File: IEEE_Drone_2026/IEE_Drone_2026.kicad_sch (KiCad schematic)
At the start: 30 parts, among them IC1 TPSM84209RKHT, IC2 TPSM84209RKHT, J1 ESC, J10 M2, J11 Conn_01x02_Socket, J2 M4 Mounting, J3 M4 Mounting, J4 M4 Mounting, J5 M4 Mounting, J6 Pixy2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

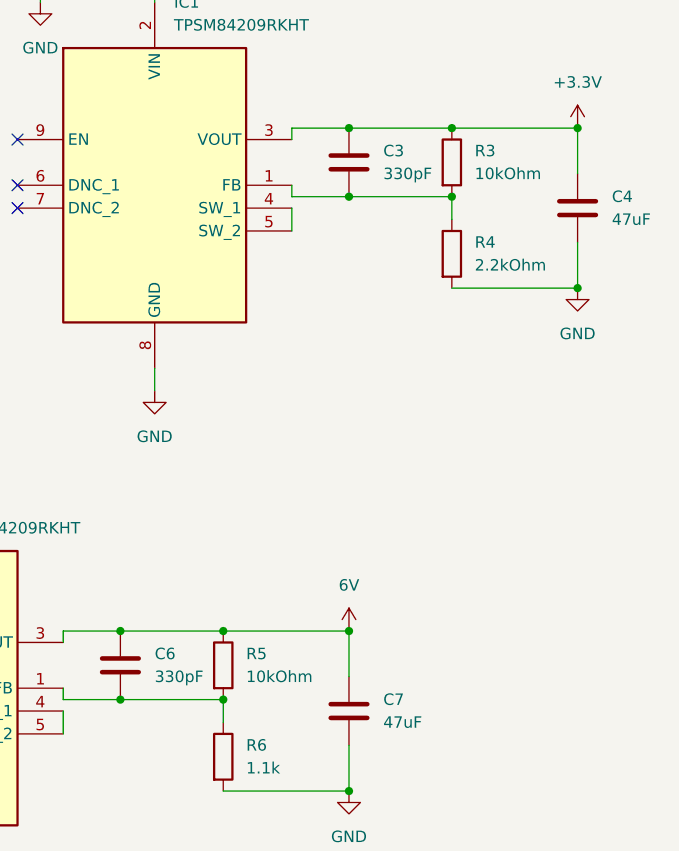
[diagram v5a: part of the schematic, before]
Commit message: updated c4 c5 c7 to 1206
coudn't find 0603 in spec
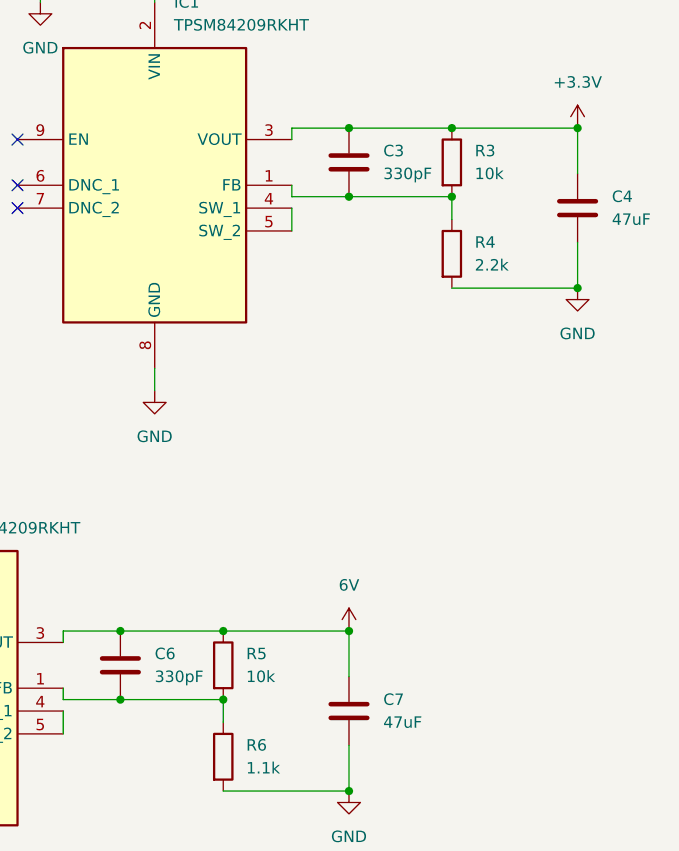
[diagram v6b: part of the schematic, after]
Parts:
- C4, C5, C7: footprint Capacitor_SMD:C_0603_1608Metric_Pad1.08x0.95mm_HandSolder -> Capacitor_SMD:C_1206_3216Metric_Pad1.33x1.80mm_HandSolder
- J1, J10, J11, J2, J3, J4, J5, J6, J7, J8, J9: now left out of the parts list
- Q1: footprint Package_TO_SOT_THT:TO-39-3 -> 2n2222:SOT95P237X111-3N
- R3, R5: value 10kOhm -> 10k
- R4: value 2.2kOhm -> 2.2k
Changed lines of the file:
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@@
 		(unit 1)
 		(exclude_from_sim no)
-		(in_bom yes)
+		(in_bom no)
 		(on_board yes)
 		(dnp no)
@@
 			)
 		)
-		(property "Footprint" "Capacitor_SMD:C_0603_1608Metric_Pad1.08x0.95mm_HandSolder"
+		(property "Footprint" "Capacitor_SMD:C_1206_3216Metric_Pad1.33x1.80mm_HandSolder"
 			(at 200.66 108.2548 0)
 			(effects
@@
 		(unit 1)
 		(exclude_from_sim no)
-		(in_bom yes)
+		(in_bom no)
 		(on_board yes)
 		(dnp no)
@@
 		(unit 1)
 		(exclude_from_sim no)
-		(in_bom yes)
+		(in_bom no)
 		(on_board yes)
 		(dnp no)
@@
 			)
 		)
-		(property "Value" "2.2kOhm"
+		(property "Value" "2.2k"
 			(at 264.16 85.0899 0)
 			(effects
@@
 		(unit 1)
 		(exclude_from_sim no)
-		(in_bom yes)
+		(in_bom no)
 		(on_board yes)
 		(dnp no)
@@
 			)
 		)
-		(property "Footprint" "Package_TO_SOT_THT:TO-39-3"
+		(property "Footprint" "2n2222:SOT95P237X111-3N"
 			(at 128.27 170.815 0)
 			(effects
@@
 		(unit 1)
 		(exclude_from_sim no)
-		(in_bom yes)
+		(in_bom no)
 		(on_board yes)
 		(dnp no)
@@
 			)
 		)
-		(property "Footprint" "Capacitor_SMD:C_0603_1608Metric_Pad1.08x0.95mm_HandSolder"
+		(property "Footprint" "Capacitor_SMD:C_1206_3216Metric_Pad1.33x1.80mm_HandSolder"
 			(at 251.1552 138.43 0)
 			(effects
@@
 		(unit 1)
 		(exclude_from_sim no)
-		(in_bom yes)
+		(in_bom no)
 		(on_board yes)
 		(dnp no)
@@
 		(unit 1)
 		(exclude_from_sim no)
-		(in_bom yes)
+		(in_bom no)
 		(on_board yes)
 		(dnp no)
@@
 		(unit 1)
 		(exclude_from_sim no)
-		(in_bom yes)
+		(in_bom no)
 		(on_board yes)
 		(dnp no)
@@
 			)
 		)
-		(property "Value" "10kOhm"
+		(property "Value" "10k"
 			(at 264.16 74.9299 0)
 			(effects
@@
 		(unit 1)
 		(exclude_from_sim no)
-		(in_bom yes)
+		(in_bom no)
 		(on_board yes)
 		(dnp no)
@@
 		(unit 1)
 		(exclude_from_sim no)
-		(in_bom yes)
+		(in_bom no)
 		(on_board yes)
 		(dnp no)
@@
 			)
 		)
-		(property "Footprint" "Capacitor_SMD:C_0603_1608Metric_Pad1.08x0.95mm_HandSolder"
+		(property "Footprint" "Capacitor_SMD:C_1206_3216Metric_Pad1.33x1.80mm_HandSolder"
 			(at 276.5552 82.55 0)
 			(effects
@@
 			)
 		)
-		(property "Value" "10kOhm"
+		(property "Value" "10k"
 			(at 238.76 130.8099 0)
 			(effects
@@
 		(unit 1)
 		(exclude_from_sim no)
-		(in_bom yes)
+		(in_bom no)
 		(on_board yes)
 		(dnp no)

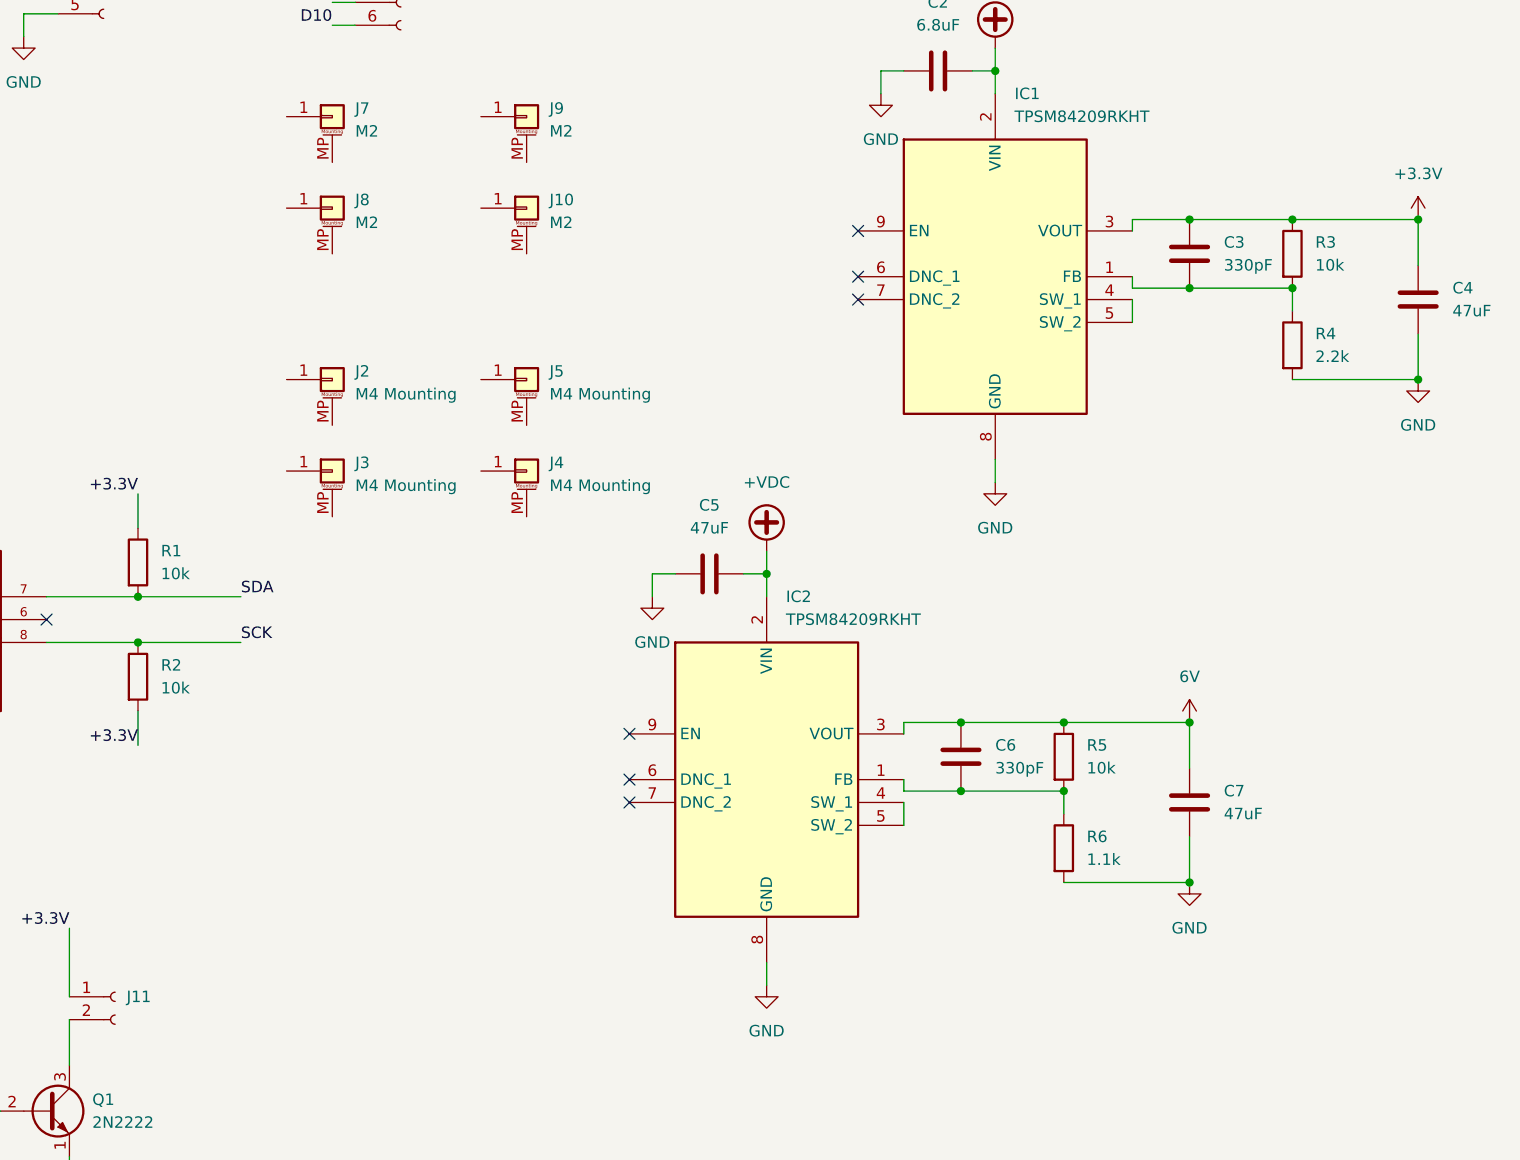
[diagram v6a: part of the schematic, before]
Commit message: added a switch for VDC
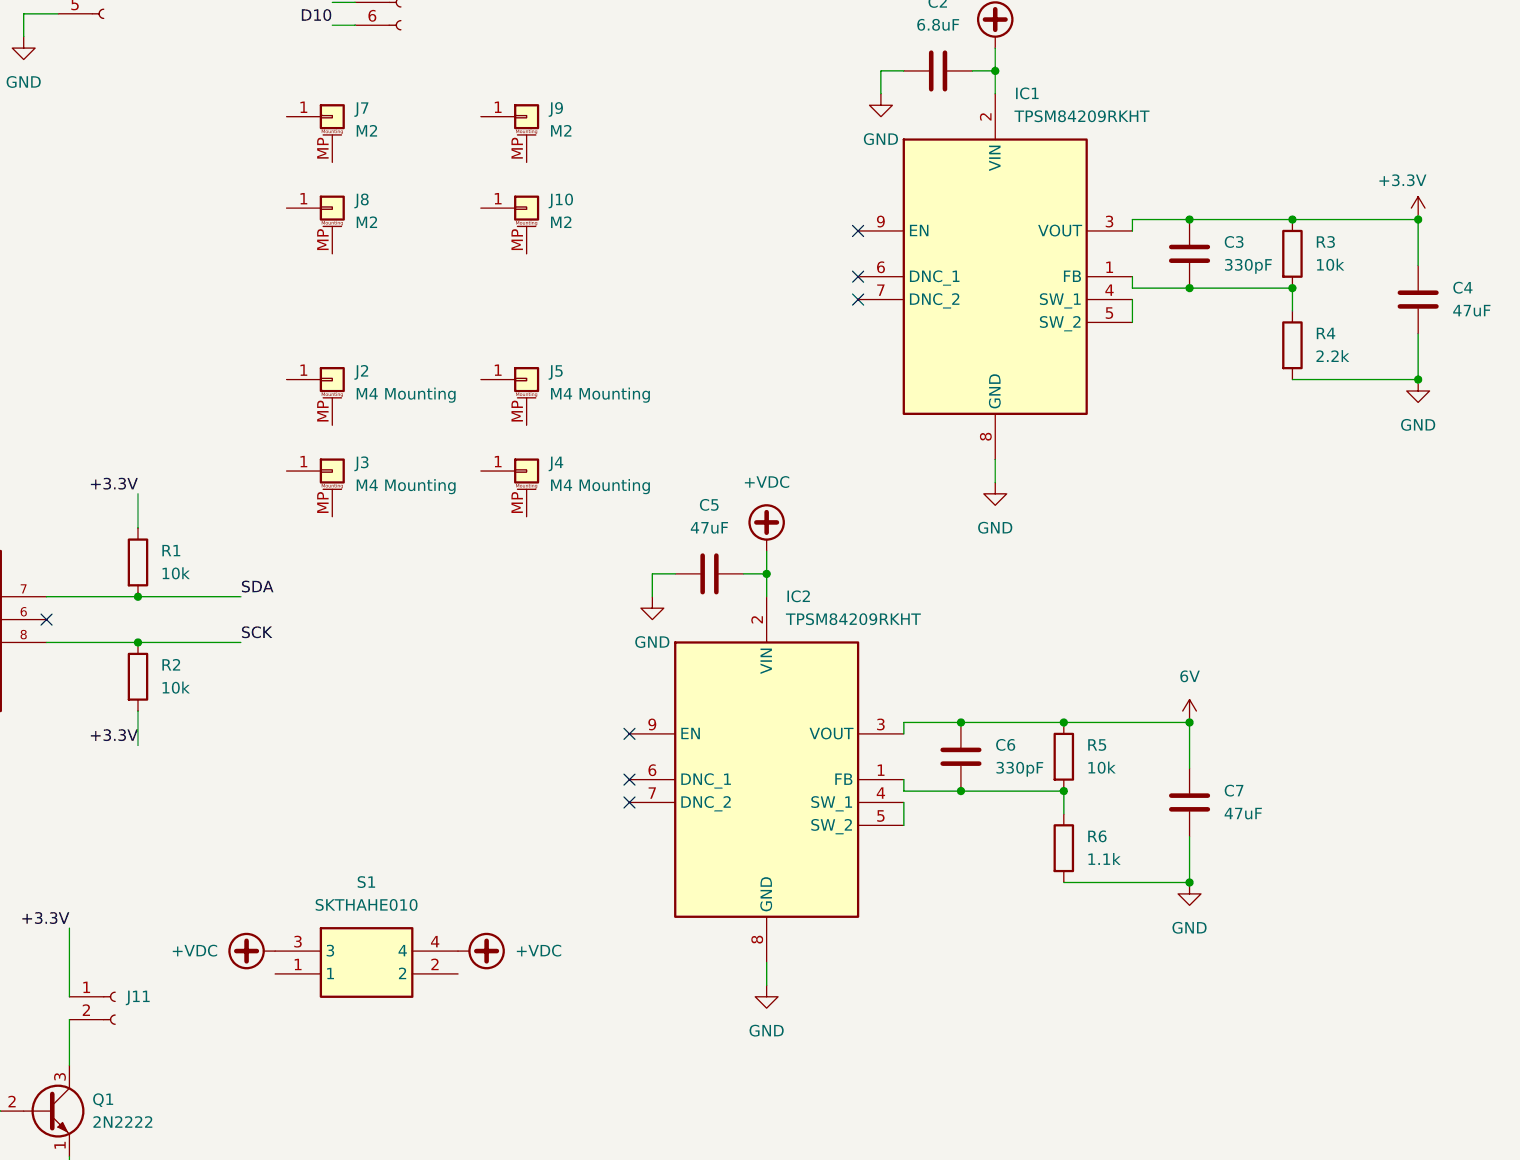
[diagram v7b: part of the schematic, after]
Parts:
- added S1: SKTHAHE010, SKTHAHE010, symbol 16vbig:SKTHAHE010
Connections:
- net +VDC: now also S1.3, S1.4

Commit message: update sch last time before redesign
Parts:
- added U2: ATSAMD21G18A-A, Package_QFP:TQFP-48_7x7mm_P0.5mm, symbol MCU_Microchip_SAMD:ATSAMD21G18A-A
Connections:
- new net: U2.18 (GND), U2.35 (GND), U2.42 (GND)
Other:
- moved on the sheet: C1, C2, C3, C4, C5, C6, C7, IC1, IC2, J1, J10, J11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
